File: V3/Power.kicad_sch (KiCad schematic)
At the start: 22 parts, among them J2 2-3S_LiPo_LARGE_HOLE_XT-30, Q1 Si2301CDS, Q2 Si2301CDS, Q3 Si2301CDS, SW1 SW_SPDT, U5 LM393, U6 ADR5040ARTZ-2.048, U7 AMS1117-3.3

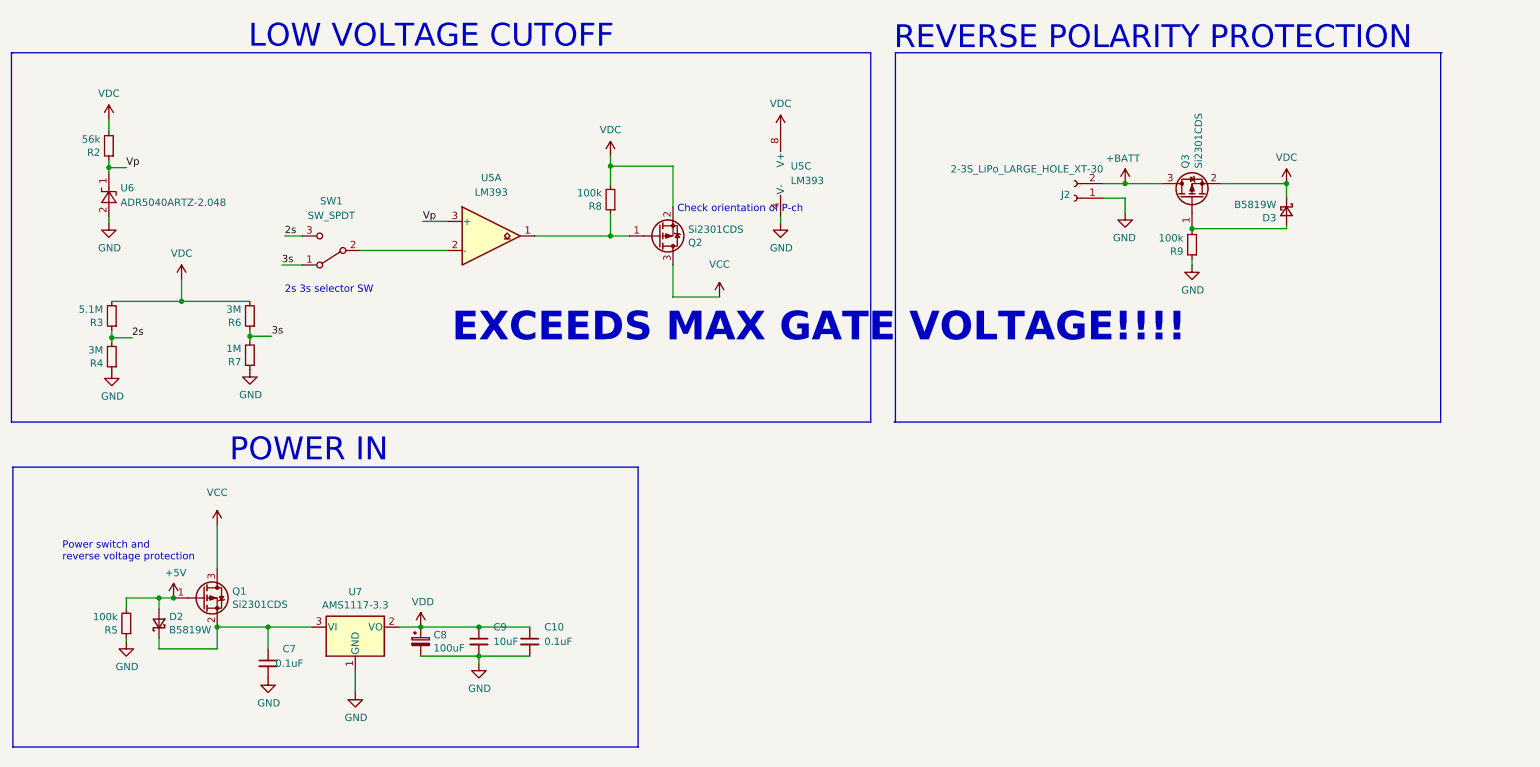
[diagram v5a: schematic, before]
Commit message: New parts placed and routed
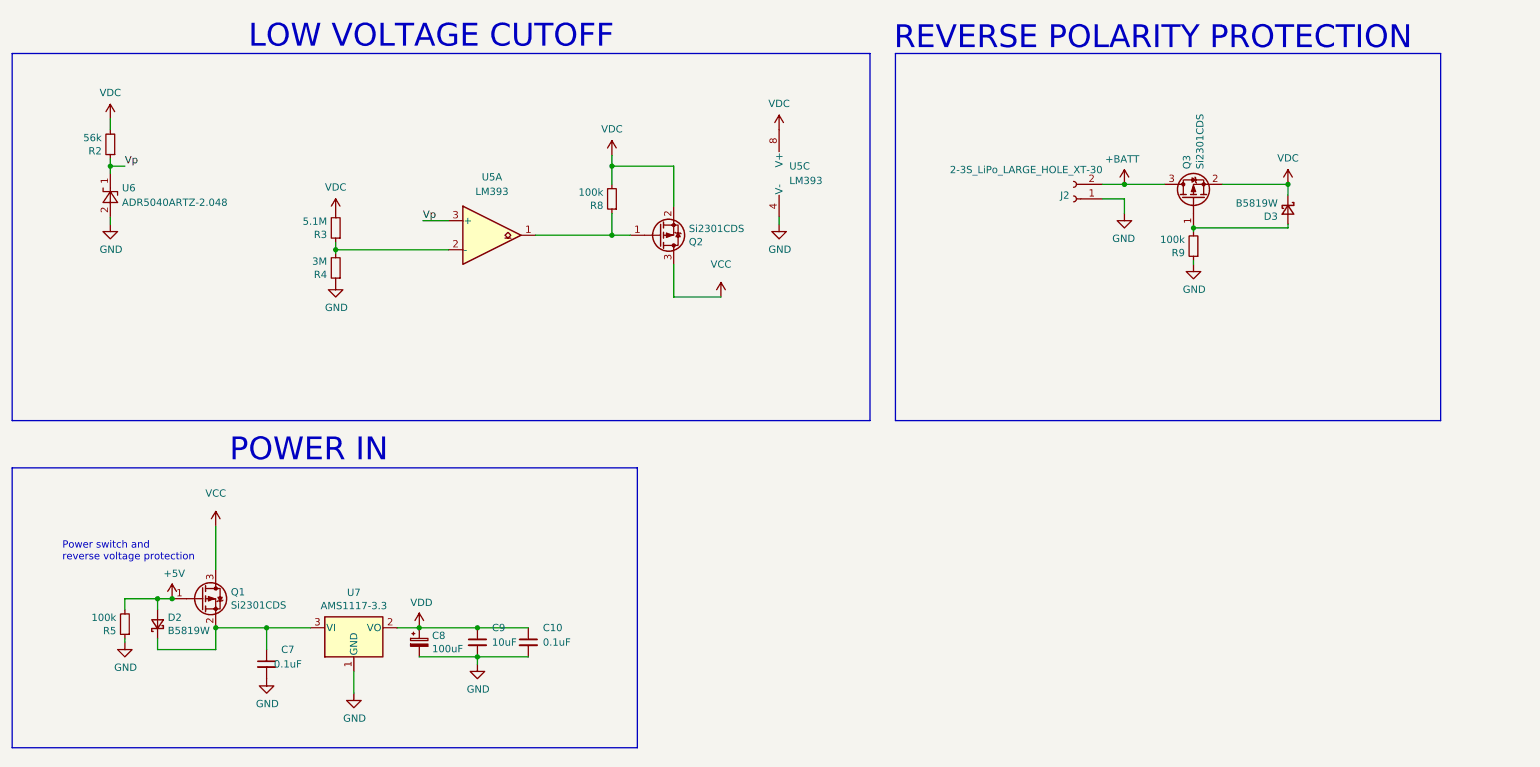
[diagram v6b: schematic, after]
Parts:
- removed R6: 3M, Resistor_SMD:R_0603_1608Metric, symbol Device:R_Small
- removed R7: 1M, Resistor_SMD:R_0603_1608Metric, symbol Device:R_Small
- removed SW1: SW_SPDT, Local_footprints:SSSS811101, symbol Switch:SW_SPDT
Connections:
- net 2s is gone; now on an unnamed net: R3.1, R4.2
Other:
- note removed: "2s 3s selector SW"
- note removed: "Check orientation of P-ch"
- note removed: "EXCEEDS MAX GATE VOLTAGE!!!!"
- moved on the sheet: R3, R4
